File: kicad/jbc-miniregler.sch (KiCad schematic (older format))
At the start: 26 parts, among them SW1 UP, SW2 DOWN, SW3 ENTER, SW4 BACK, U1 OLED-128x32-Module, X1 POWER, X2 COM, X3 Lötkolben

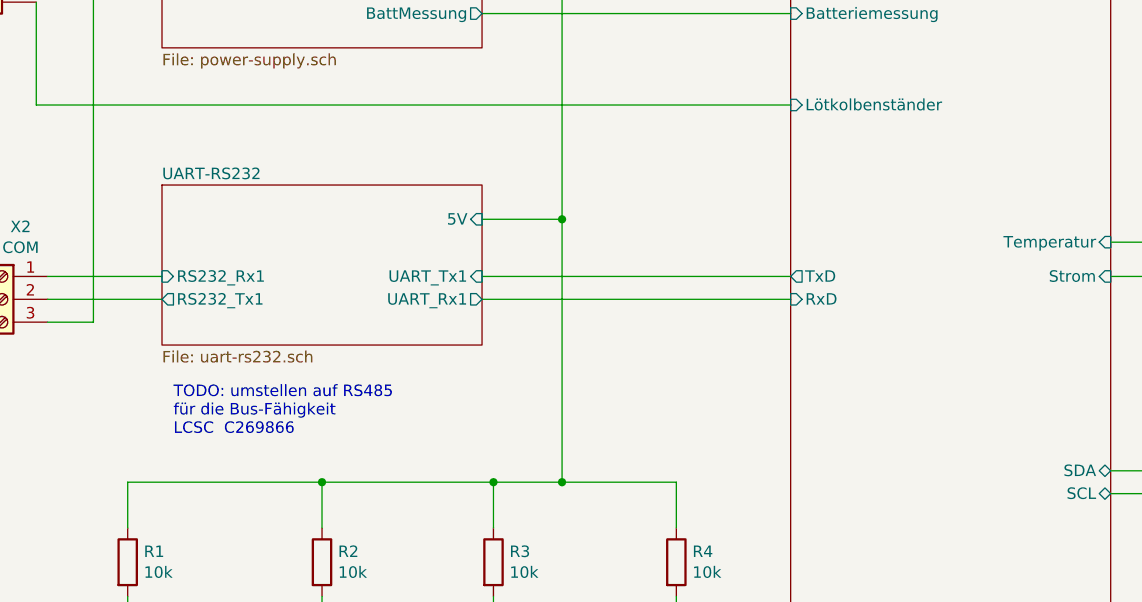
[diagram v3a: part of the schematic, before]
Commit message: um Option RS485 erweitert
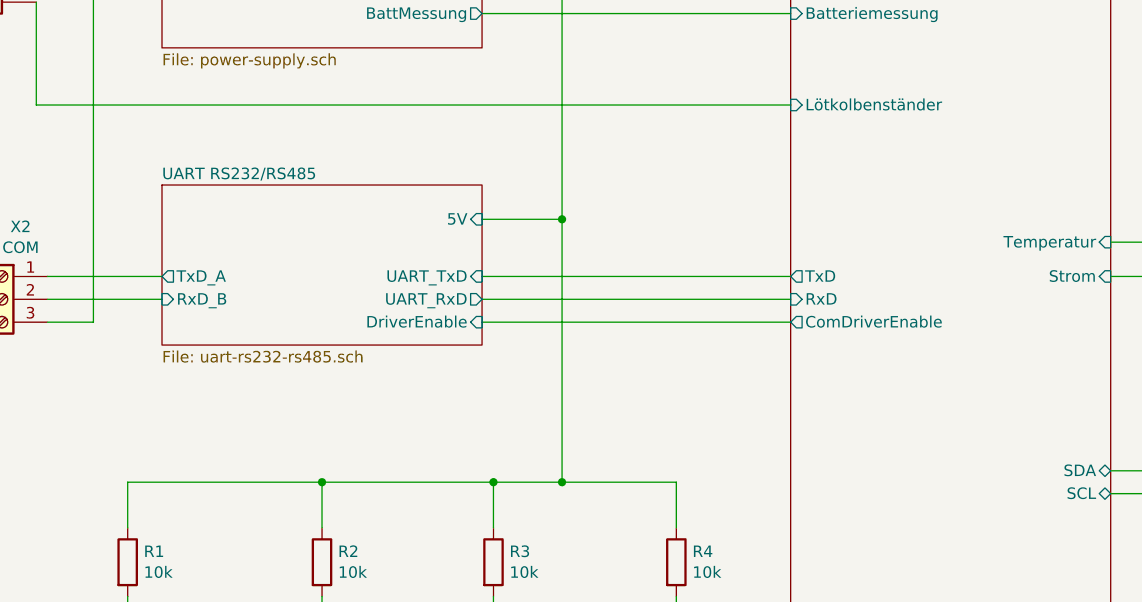
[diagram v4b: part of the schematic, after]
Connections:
- net UART-RS232/RS232_Rx1 renamed UART RS232/RS485/TxD_A
- net UART-RS232/RS232_Tx1 renamed UART RS232/RS485/RxD_B
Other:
- note removed: "TODO: umstellen auf RS485\nfür die Bus-Fähigkeit\nLCSC C269866"
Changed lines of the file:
@@
 F16 "SDA" B R 5950 4400 50
 F17 "Lötkolbenständer" I L 4550 2800 50
+F18 "ComDriverEnable" O L 4550 3750 50
 $EndSheet
 $Sheet
@@
 S 1800 3150 1400 700
 U 60A756E2
-F0 "UART-RS232" 50
-F1 "uart-rs232.sch" 50
-F2 "UART_Tx1" I R 3200 3550 50
-F3 "UART_Rx1" O R 3200 3650 50
-F4 "RS232_Rx1" I L 1800 3550 50
-F5 "RS232_Tx1" O L 1800 3650 50
-F6 "5V" I R 3200 3300 50
+F0 "UART RS232/RS485" 50
+F1 "uart-rs232-rs485.sch" 50
+F2 "5V" I R 3200 3300 50
+F3 "UART_TxD" I R 3200 3550 50
+F4 "RxD_B" I L 1800 3650 50
+F5 "UART_RxD" O R 3200 3650 50
+F6 "DriverEnable" I R 3200 3750 50
+F7 "TxD_A" O L 1800 3550 50
 $EndSheet
 $Comp
@@
 Wire Wire Line
 	1500 2250 1800 2250
-Text Notes 1850 4250 0    50   ~ 0
-TODO: umstellen auf RS485\nfür die Bus-Fähigkeit\nLCSC  C269866
 Text Label 3750 2300 0    50   ~ 0
 5V
@@
 Text Notes 8200 2350 0    50   ~ 0
 TODO: Footprint\nHier gibts noch ein problem mit der x-Ausrichtung\nDas 3D-Modell passt offenbar nicht zu 2D-Skizze\nPins sollten zum Drahtloch leicht versetzt sein.
+Wire Wire Line
+	3200 3750 4550 3750
 $EndSCHEMATC

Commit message: Bestellte Version v21.0.0
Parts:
- removed H1, H2, H3, H4: MountingHole, htl_mechanical:mountinghole_d4mm_R5mm, symbol Mechanical:MountingHole
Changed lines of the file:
@@
 encoding utf-8
 Sheet 1 10
-Title "JBC-Miniregler"
-Date "2021-05-02"
-Rev "0.0.1"
+Title "HTL Lötregler Mini"
+Date "2021-06-01"
+Rev "21.0.0"
 Comp "HTL Steyr"
-Comment1 "Prof. Karl Zeilhofer"
+Comment1 "Prof. Karl Zeilhofer et al."
 Comment2 ""
 Comment3 ""
@@
 	1    0    0    -1
 $EndComp
-$Comp
-L Mechanical:MountingHole H1
-U 1 1 60B4E525
-P 9950 5050
-F 0 "H1" H 10050 5096 50  0000 L CNN
-F 1 "MountingHole" H 10050 5005 50  0000 L CNN
-F 2 "htl_mechanical:mountinghole_d4mm_R5mm" H 9950 5050 50  0001 C CNN
-F 3 "~" H 9950 5050 50  0001 C CNN
-F 4 "NAP2" H 9950 5050 50  0001 C CNN "DistOrderNr"
-F 5 "NAP" H 9950 5050 50  0001 C CNN "Distributor"
-F 6 "NAP" H 9950 5050 50  0001 C CNN "ManPartNr"
-F 7 "NAP" H 9950 5050 50  0001 C CNN "Manufacturer"
-F 8 "Not a Part" H 9950 5050 50  0001 C CNN "Notes"
-F 9 "0.00" H 9950 5050 50  0001 C CNN "PriceEUR"
-	1    9950 5050
-	1    0    0    -1
-$EndComp
-$Comp
-L Mechanical:MountingHole H2
-U 1 1 60B4EA6D
-P 9950 5250
-F 0 "H2" H 10050 5296 50  0000 L CNN
-F 1 "MountingHole" H 10050 5205 50  0000 L CNN
-F 2 "htl_mechanical:mountinghole_d4mm_R5mm" H 9950 5250 50  0001 C CNN
-F 3 "~" H 9950 5250 50  0001 C CNN
-F 4 "NAP2" H 9950 5250 50  0001 C CNN "DistOrderNr"
-F 5 "NAP" H 9950 5250 50  0001 C CNN "Distributor"
-F 6 "NAP" H 9950 5250 50  0001 C CNN "ManPartNr"
-F 7 "NAP" H 9950 5250 50  0001 C CNN "Manufacturer"
-F 8 "Not a Part" H 9950 5250 50  0001 C CNN "Notes"
-F 9 "0.00" H 9950 5250 50  0001 C CNN "PriceEUR"
-	1    9950 5250
-	1    0    0    -1
-$EndComp
-$Comp
-L Mechanical:MountingHole H3
-U 1 1 60B4EC08
-P 9950 5450
-F 0 "H3" H 10050 5496 50  0000 L CNN
-F 1 "MountingHole" H 10050 5405 50  0000 L CNN
-F 2 "htl_mechanical:mountinghole_d4mm_R5mm" H 9950 5450 50  0001 C CNN
-F 3 "~" H 9950 5450 50  0001 C CNN
-F 4 "NAP2" H 9950 5450 50  0001 C CNN "DistOrderNr"
-F 5 "NAP" H 9950 5450 50  0001 C CNN "Distributor"
-F 6 "NAP" H 9950 5450 50  0001 C CNN "ManPartNr"
-F 7 "NAP" H 9950 5450 50  0001 C CNN "Manufacturer"
-F 8 "Not a Part" H 9950 5450 50  0001 C CNN "Notes"
-F 9 "0.00" H 9950 5450 50  0001 C CNN "PriceEUR"
-	1    9950 5450
-	1    0    0    -1
-$EndComp
-$Comp
-L Mechanical:MountingHole H4
-U 1 1 60B4EDEA
-P 9950 5650
-F 0 "H4" H 10050 5696 50  0000 L CNN
-F 1 "MountingHole" H 10050 5605 50  0000 L CNN
-F 2 "htl_mechanical:mountinghole_d4mm_R5mm" H 9950 5650 50  0001 C CNN
-F 3 "~" H 9950 5650 50  0001 C CNN
-F 4 "NAP2" H 9950 5650 50  0001 C CNN "DistOrderNr"
-F 5 "NAP" H 9950 5650 50  0001 C CNN "Distributor"
-F 6 "NAP" H 9950 5650 50  0001 C CNN "ManPartNr"
-F 7 "NAP" H 9950 5650 50  0001 C CNN "Manufacturer"
-F 8 "Not a Part" H 9950 5650 50  0001 C CNN "Notes"
-F 9 "0.00" H 9950 5650 50  0001 C CNN "PriceEUR"
-	1    9950 5650
-	1    0    0    -1
-$EndComp

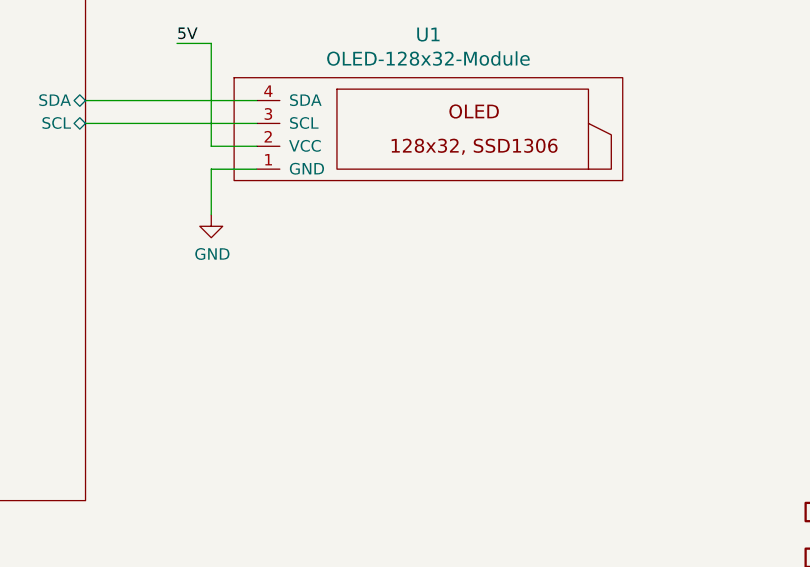
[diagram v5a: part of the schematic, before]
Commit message: Buchsenleist für OLED hinzugefügt
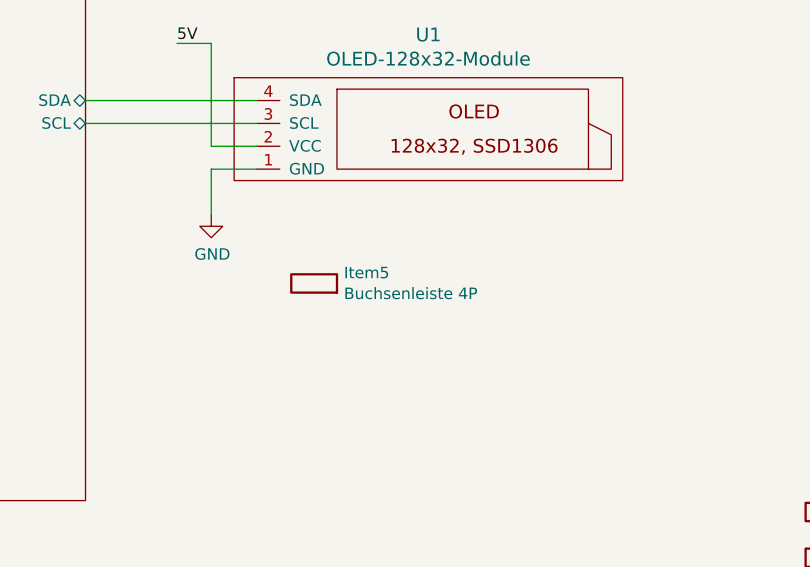
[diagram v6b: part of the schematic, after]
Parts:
- added Item5: Buchsenleiste 4P, htl_virtual:Virtual-Item, symbol htl_virtual:Item
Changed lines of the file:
@@
 Wire Wire Line
 	3200 3750 4550 3750
+$Comp
+L htl_virtual:Item Item5
+U 1 1 60C20DEA
+P 6950 5200
+F 0 "Item5" H 7080 5246 50  0000 L CNN
+F 1 "Buchsenleiste 4P" H 7080 5155 50  0000 L CNN
+F 2 "htl_virtual:Virtual-Item" H 6950 5130 50  0001 C CNN
+F 3 "~" V 6950 5200 50  0001 C CNN
+F 4 "CJT(Changjiang Connectors)" H 6950 5200 50  0001 C CNN "Manufacturer"
+F 5 "A2541HWV-4P" H 6950 5200 50  0001 C CNN "ManPartNr"
+F 6 "LCSC" H 6950 5200 50  0001 C CNN "Distributor"
+F 7 "C225501" H 6950 5200 50  0001 C CNN "DistOrderNr"
+F 8 "0.0517" H 6950 5200 50  0001 C CNN "PriceEUR"
+F 9 "50" H 6950 5200 50  0001 C CNN "PriceForQty"
+F 10 "https://lcsc.com/product-detail/Pin-Header-Female-Header_CJT-Changjiang-Connectors-A2541HWV-4P_C225501.html" H 6950 5200 50  0001 C CNN "Weblink"
+F 11 "Buchsenleiste, 8.5mm hoch, 2.54mm Raster" H 6950 5200 50  0001 C CNN "Notes"
+	1    6950 5200
+	1    0    0    -1
+$EndComp
 $EndSCHEMATC

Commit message: wip, bugfixes für v21.0.1
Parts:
- R2, R3, R4: Notes (none) -> 10kΩ ±5% 0.25W ±100ppm/℃ 3216 Chip Resistor
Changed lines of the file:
@@
 Sheet 1 10
 Title "HTL Lötregler Mini"
-Date "2021-06-01"
-Rev "21.0.0"
+Date "2021-09-22"
+Rev "21.0.1-dev"
 Comp "HTL Steyr"
 Comment1 "Prof. Karl Zeilhofer et al."
@@
 F 5 "C118075" H 3250 4800 50  0001 C CNN "DistOrderNr"
 F 6 "LCSC" H 3250 4800 50  0001 C CNN "Distributor"
+F 7 "10kΩ ±5% 0.25W ±100ppm/℃ 3216 Chip Resistor" H 3250 4800 50  0001 C CNN "Notes"
 	1    3250 4800
 	1    0    0    -1
@@
 F 5 "C118075" H 4050 4800 50  0001 C CNN "DistOrderNr"
 F 6 "LCSC" H 4050 4800 50  0001 C CNN "Distributor"
+F 7 "10kΩ ±5% 0.25W ±100ppm/℃ 3216 Chip Resistor" H 4050 4800 50  0001 C CNN "Notes"
 	1    4050 4800
 	1    0    0    -1
@@
 F 5 "C118075" H 2500 4800 50  0001 C CNN "DistOrderNr"
 F 6 "LCSC" H 2500 4800 50  0001 C CNN "Distributor"
+F 7 "10kΩ ±5% 0.25W ±100ppm/℃ 3216 Chip Resistor" H 2500 4800 50  0001 C CNN "Notes"
 	1    2500 4800
 	1    0    0    -1

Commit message: BOM aktualisiert, Zenerdiode: Pinout IPC-konform gestaltet, ...
siehe https://gitlab.com/kicad/libraries/kicad-symbols/-/issues/3157
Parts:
- C1, C2, C3, C4: Index (none) -> 40
- D1: Index (none) -> 46
- FID1, FID2: Index (none) -> 52
- Item1: Index (none) -> 50; PriceEUR 0.1656 -> 0.53; PriceForQty 100 -> 40
- Item2: Index (none) -> 51; PriceEUR 3.71 -> 3.55; PriceForQty 100 -> 40
- Item5: Index (none) -> 25
- R1, R2, R3, R4: Index (none) -> 15
- R5: Index (none) -> 12
- SW1, SW2, SW3, SW4: Index (none) -> 33
- U1: Index (none) -> 55
- X1, X2, X3: Index (none) -> 41
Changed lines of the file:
@@
 F 7 "100" H 8550 1850 50  0001 C CNN "PriceForQty"
 F 8 "3 poles, 5.08mm, 15A 250V AWG14~22 1.5mm² P=5.08mm Spring Clamp System Terminal Block" H 8550 1850 50  0001 C CNN "Notes"
+F 9 "41" H 8550 1850 50  0001 C CNN "Index"
 	1    8550 1850
 	1    0    0    1
@@
 F 7 "100" H 1100 3650 50  0001 C CNN "PriceForQty"
 F 8 "3 poles, 5.08mm, 15A 250V AWG14~22 1.5mm² P=5.08mm Spring Clamp System Terminal Block" H 1100 3650 50  0001 C CNN "Notes"
+F 9 "41" H 1100 3650 50  0001 C CNN "Index"
 	1    1100 3650
 	-1   0    0    -1
@@
 F 10 "500" H 3250 6000 50  0001 C CNN "PriceForQty"
 F 11 "https://lcsc.com/product-detail/Tactile-Switches_XKB-Connectivity-TS-1187A-B-A-B_C318884.html" H 3250 6000 50  0001 C CNN "Weblink"
+F 12 "33" H 3250 6000 50  0001 C CNN "Index"
 	1    3250 6000
 	0    -1   -1   0
@@
 F 10 "500" H 4050 6000 50  0001 C CNN "PriceForQty"
 F 11 "https://lcsc.com/product-detail/Tactile-Switches_XKB-Connectivity-TS-1187A-B-A-B_C318884.html" H 4050 6000 50  0001 C CNN "Weblink"
+F 12 "33" H 4050 6000 50  0001 C CNN "Index"
 	1    4050 6000
 	0    -1   -1   0
@@
 F 6 "LCSC" H 3250 4800 50  0001 C CNN "Distributor"
 F 7 "10kΩ ±5% 0.25W ±100ppm/℃ 3216 Chip Resistor" H 3250 4800 50  0001 C CNN "Notes"
+F 8 "15" H 3250 4800 50  0001 C CNN "Index"
 	1    3250 4800
 	1    0    0    -1
@@
 F 6 "LCSC" H 4050 4800 50  0001 C CNN "Distributor"
 F 7 "10kΩ ±5% 0.25W ±100ppm/℃ 3216 Chip Resistor" H 4050 4800 50  0001 C CNN "Notes"
+F 8 "15" H 4050 4800 50  0001 C CNN "Index"
 	1    4050 4800
 	1    0    0    -1
@@
 F 10 "500" H 1650 6000 50  0001 C CNN "PriceForQty"
 F 11 "https://lcsc.com/product-detail/Tactile-Switches_XKB-Connectivity-TS-1187A-B-A-B_C318884.html" H 1650 6000 50  0001 C CNN "Weblink"
+F 12 "33" H 1650 6000 50  0001 C CNN "Index"
 	1    1650 6000
 	0    -1   -1   0
@@
 F 10 "500" H 2500 6000 50  0001 C CNN "PriceForQty"
 F 11 "https://lcsc.com/product-detail/Tactile-Switches_XKB-Connectivity-TS-1187A-B-A-B_C318884.html" H 2500 6000 50  0001 C CNN "Weblink"
+F 12 "33" H 2500 6000 50  0001 C CNN "Index"
 	1    2500 6000
 	0    -1   -1   0
@@
 F 6 "LCSC" H 1650 4800 50  0001 C CNN "Distributor"
 F 7 "10kΩ ±5% 0.25W ±100ppm/℃ 3216 Chip Resistor" H 1650 4800 50  0001 C CNN "Notes"
+F 8 "15" H 1650 4800 50  0001 C CNN "Index"
 	1    1650 4800
 	1    0    0    -1
@@
 F 6 "LCSC" H 2500 4800 50  0001 C CNN "Distributor"
 F 7 "10kΩ ±5% 0.25W ±100ppm/℃ 3216 Chip Resistor" H 2500 4800 50  0001 C CNN "Notes"
+F 8 "15" H 2500 4800 50  0001 C CNN "Index"
 	1    2500 4800
 	1    0    0    -1
@@
 F 7 "0.0079" H 6200 2550 50  0001 C CNN "PriceEUR"
 F 8 "50" H 6200 2550 50  0001 C CNN "PriceForQty"
+F 9 "46" H 6200 2550 50  0001 C CNN "Index"
 	1    6200 2550
 	0    -1   -1   0
@@
 F 9 "1kΩ ±5% 0.25W ±100ppm/℃ 1206 Chip Resistor" H 6200 2150 50  0001 C CNN "Notes"
 F 10 "50" H 6200 2150 50  0001 C CNN "PriceForQty"
+F 11 "12" H 6200 2150 50  0001 C CNN "Index"
 	1    6200 2150
 	1    0    0    -1
@@
 F 10 "500" H 1800 5700 50  0001 C CNN "PriceForQty"
 F 11 "" H 1800 5700 50  0001 C CNN "Weblink"
+F 12 "40" H 1800 5700 50  0001 C CNN "Index"
+F 13 "" H 1800 5700 50  0001 C CNN "NotesAlt"
 	1    1800 5700
 	0    1    1    0
@@
 F 10 "500" H 2650 5700 50  0001 C CNN "PriceForQty"
 F 11 "" H 2650 5700 50  0001 C CNN "Weblink"
+F 12 "40" H 2650 5700 50  0001 C CNN "Index"
+F 13 "" H 2650 5700 50  0001 C CNN "NotesAlt"
 	1    2650 5700
 	0    1    1    0
@@
 F 10 "500" H 3400 5700 50  0001 C CNN "PriceForQty"
 F 11 "" H 3400 5700 50  0001 C CNN "Weblink"
+F 12 "40" H 3400 5700 50  0001 C CNN "Index"
+F 13 "" H 3400 5700 50  0001 C CNN "NotesAlt"
 	1    3400 5700
 	0    1    1    0
@@
 F 10 "500" H 4200 5700 50  0001 C CNN "PriceForQty"
 F 11 "" H 4200 5700 50  0001 C CNN "Weblink"
+F 12 "40" H 4200 5700 50  0001 C CNN "Index"
+F 13 "" H 4200 5700 50  0001 C CNN "NotesAlt"
 	1    4200 5700
 	0    1    1    0
@@
 F 8 "OLED, 128x32, 23mm, I2C, 3.3/5V, weiß, SSD1306" H 7450 4500 50  0001 C CNN "Notes"
 F 9 "OLED_128x64_white" H 7450 4500 50  0001 C CNN "DistOrderNr"
+F 10 "55" H 7450 4500 50  0001 C CNN "Index"
 	1    7450 4500
 	1    0    0    -1
@@
 F 5 "Multi-CB" H 9200 6400 50  0001 C CNN "Distributor"
 F 6 "Multi-CB" H 9200 6400 50  0001 C CNN "Manufacturer"
-F 7 "3.71" H 9200 6400 50  0001 C CNN "PriceEUR"
-F 8 "100" H 9200 6400 50  0001 C CNN "PriceForQty"
+F 7 "3.55" H 9200 6400 50  0001 C CNN "PriceEUR"
+F 8 "40" H 9200 6400 50  0001 C CNN "PriceForQty"
+F 9 "51" H 9200 6400 50  0001 C CNN "Index"
 	1    9200 6400
 	1    0    0    -1
@@
 F 5 "Multi-CB" H 9200 6200 50  0001 C CNN "Distributor"
 F 6 "Multi-CB" H 9200 6200 50  0001 C CNN "Manufacturer"
-F 7 "0.1656" H 9200 6200 50  0001 C CNN "PriceEUR"
-F 8 "100" H 9200 6200 50  0001 C CNN "PriceForQty"
+F 7 "0.53" H 9200 6200 50  0001 C CNN "PriceEUR"
+F 8 "40" H 9200 6200 50  0001 C CNN "PriceForQty"
+F 9 "50" H 9200 6200 50  0001 C CNN "Index"
 	1    9200 6200
 	1    0    0    -1
@@
 F 6 "0.00" H 9950 4650 50  0001 C CNN "PriceEUR"
 F 7 "NAP" H 9950 4650 50  0001 C CNN "Distributor"
+F 8 "52" H 9950 4650 50  0001 C CNN "Index"
 	1    9950 4650
 	1    0    0    -1
@@
 F 6 "0.00" H 9950 4450 50  0001 C CNN "PriceEUR"
 F 7 "NAP" H 9950 4450 50  0001 C CNN "Distributor"
+F 8 "52" H 9950 4450 50  0001 C CNN "Index"
 	1    9950 4450
 	1    0    0    -1
@@
 F 7 "100" H 1050 2250 50  0001 C CNN "PriceForQty"
 F 8 "3 poles, 5.08mm, 15A 250V AWG14~22 1.5mm² P=5.08mm Spring Clamp System Terminal Block" H 1050 2250 50  0001 C CNN "Notes"
+F 9 "41" H 1050 2250 50  0001 C CNN "Index"
 	1    1050 2250
 	-1   0    0    -1
@@
 F 10 "https://lcsc.com/product-detail/Pin-Header-Female-Header_CJT-Changjiang-Connectors-A2541HWV-4P_C225501.html" H 6950 5200 50  0001 C CNN "Weblink"
 F 11 "Buchsenleiste, 8.5mm hoch, 2.54mm Raster" H 6950 5200 50  0001 C CNN "Notes"
+F 12 "25" H 6950 5200 50  0001 C CNN "Index"
 	1    6950 5200
 	1    0    0    -1
